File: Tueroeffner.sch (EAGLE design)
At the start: 34 parts, among them IC1 NCP1117ST33T3G, IC3 M25PE20, K1 EC2-12SNU, Q1 2N7002CK, Q3 2N7002CK

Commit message: New H-Bridge
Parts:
- removed D3, D4: PMBD914, semicon-smd-ipc:D-A1-C3
- added Q2, Q4: 2N7002CK, SparkFun-DiscreteSemi:MOSFET-NCHANNELBSS123LT1G
- added R8, R9: 100, resistor:R-EU_M2012
- R4, R5: value 47 -> 10K
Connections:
- new net N$4: R8.2, U$5.(ZEROX/IO/ADC3)P14
- new net N$5: R9.2, U$5.(TRIAC/IO/ADC2)P13
- net DC_5-12V: now also Q2.D, Q4.D; no longer D3.C, D4.C, R4.2, R5.2
- net GND: now also R4.1, R5.1
- net N$2: now also Q2.S; no longer D3.A, R4.1
- net N$3: now also Q4.S; no longer D4.A, R5.1
- net RELAY0: now also Q2.G, R4.2, R8.1; no longer U$5.(ZEROX/IO/ADC3)P14
- net RELAY1: now also Q4.G, R5.2, R9.1; no longer U$5.(TRIAC/IO/ADC2)P13
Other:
- moved on the sheet: K1, Q1, Q3, R4, R5, R6, R7

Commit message: Basic Routing
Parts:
- removed R5, R7: 10K, resistor:R-EU_M2012
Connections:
- net GND: no longer R5.1, R7.1
- net RELAY0: no longer R7.2
- net RELAY1: no longer R5.2
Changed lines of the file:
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@@
 <part name="B1" library="rectifier" deviceset="RECTIFIER-" device="S40"/>
 <part name="R6" library="resistor" deviceset="R-EU_" device="M2012" value="10K"/>
-<part name="R7" library="resistor" deviceset="R-EU_" device="M2012" value="10K"/>
 <part name="Q3" library="SparkFun-DiscreteSemi" deviceset="MOSFET-NCHANNEL" device="BSS123LT1G" value="2N7002CK"/>
 <part name="Q1" library="SparkFun-DiscreteSemi" deviceset="MOSFET-NCHANNEL" device="BSS123LT1G" value="2N7002CK"/>
@@
 <part name="JP3" library="SparkFun-Connectors" deviceset="M04" device="SCREW"/>
 <part name="R4" library="resistor" deviceset="R-EU_" device="M2012" value="10K"/>
-<part name="R5" library="resistor" deviceset="R-EU_" device="M2012" value="10K"/>
 <part name="Q2" library="SparkFun-DiscreteSemi" deviceset="MOSFET-NCHANNEL" device="BSS123LT1G" value="2N7002CK"/>
 <part name="Q4" library="SparkFun-DiscreteSemi" deviceset="MOSFET-NCHANNEL" device="BSS123LT1G" value="2N7002CK"/>
 <part name="GND8" library="supply1" deviceset="GND" device=""/>
-<part name="GND9" library="supply1" deviceset="GND" device=""/>
 <part name="GND10" library="supply1" deviceset="GND" device=""/>
 <part name="R8" library="resistor" deviceset="R-EU_" device="M2012" value="100"/>
@@
 <attribute name="VALUE" x="262.382" y="-6.35" size="1.778" layer="96" rot="R90"/>
 </instance>
-<instance part="R7" gate="G$1" x="281.94" y="-2.54" smashed="yes" rot="R90">
-<attribute name="NAME" x="280.4414" y="-6.35" size="1.778" layer="95" rot="R90"/>
-<attribute name="VALUE" x="285.242" y="-6.35" size="1.778" layer="96" rot="R90"/>
-</instance>
 <instance part="Q3" gate="G$1" x="269.24" y="5.08" smashed="yes">
 <attribute name="NAME" x="270.51" y="7.62" size="1.778" layer="95"/>
@@
 <attribute name="VALUE" x="262.382" y="24.13" size="1.778" layer="96" rot="R90"/>
 </instance>
-<instance part="R5" gate="G$1" x="281.94" y="27.94" smashed="yes" rot="R90">
-<attribute name="NAME" x="280.4414" y="24.13" size="1.778" layer="95" rot="R90"/>
-<attribute name="VALUE" x="285.242" y="24.13" size="1.778" layer="96" rot="R90"/>
-</instance>
 <instance part="Q2" gate="G$1" x="269.24" y="35.56" smashed="yes">
 <attribute name="NAME" x="270.51" y="38.1" size="1.778" layer="95"/>
@@
 <instance part="GND8" gate="1" x="259.08" y="17.78" smashed="yes">
 <attribute name="VALUE" x="256.54" y="15.24" size="1.778" layer="96"/>
-</instance>
-<instance part="GND9" gate="1" x="281.94" y="17.78" smashed="yes">
-<attribute name="VALUE" x="279.4" y="15.24" size="1.778" layer="96"/>
 </instance>
 <instance part="GND10" gate="1" x="259.08" y="-15.24" smashed="yes">
@@
 <wire x1="281.94" y1="-12.7" x2="281.94" y2="-10.16" width="0.1524" layer="91"/>
 <junction x="281.94" y="-10.16"/>
-<pinref part="R7" gate="G$1" pin="1"/>
-<wire x1="281.94" y1="-7.62" x2="281.94" y2="-10.16" width="0.1524" layer="91"/>
 <junction x="281.94" y="-10.16"/>
 <pinref part="Q3" gate="G$1" pin="S"/>
@@
 <pinref part="R4" gate="G$1" pin="1"/>
 <wire x1="259.08" y1="20.32" x2="259.08" y2="22.86" width="0.1524" layer="91"/>
-</segment>
-<segment>
-<pinref part="GND9" gate="1" pin="GND"/>
-<pinref part="R5" gate="G$1" pin="1"/>
-<wire x1="281.94" y1="20.32" x2="281.94" y2="22.86" width="0.1524" layer="91"/>
 </segment>
 <segment>
@@
 </segment>
 <segment>
-<wire x1="284.48" y1="5.08" x2="281.94" y2="5.08" width="0.1524" layer="91"/>
 <label x="279.4" y="5.08" size="0.8128" layer="95" rot="R180" xref="yes"/>
-<pinref part="R7" gate="G$1" pin="2"/>
-<wire x1="281.94" y1="5.08" x2="279.4" y2="5.08" width="0.1524" layer="91"/>
-<wire x1="281.94" y1="2.54" x2="281.94" y2="5.08" width="0.1524" layer="91"/>
-<junction x="281.94" y="5.08"/>
+<wire x1="284.48" y1="5.08" x2="279.4" y2="5.08" width="0.1524" layer="91"/>
 <pinref part="Q1" gate="G$1" pin="G"/>
 </segment>
@@
 </segment>
 <segment>
-<wire x1="284.48" y1="35.56" x2="281.94" y2="35.56" width="0.1524" layer="91"/>
 <label x="279.4" y="35.56" size="0.8128" layer="95" rot="R180" xref="yes"/>
-<pinref part="R5" gate="G$1" pin="2"/>
-<wire x1="281.94" y1="35.56" x2="279.4" y2="35.56" width="0.1524" layer="91"/>
-<wire x1="281.94" y1="33.02" x2="281.94" y2="35.56" width="0.1524" layer="91"/>
-<junction x="281.94" y="35.56"/>
+<wire x1="284.48" y1="35.56" x2="279.4" y2="35.56" width="0.1524" layer="91"/>
 <pinref part="Q4" gate="G$1" pin="G"/>
 </segment>

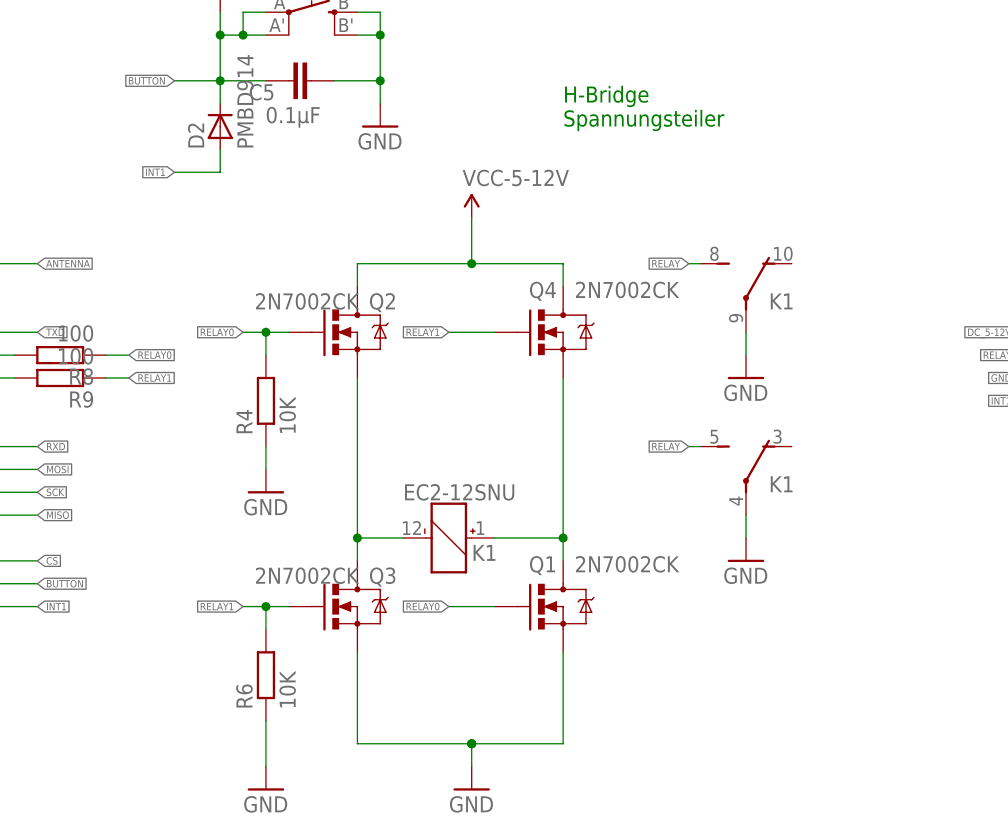
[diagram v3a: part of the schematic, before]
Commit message: New Relais designe
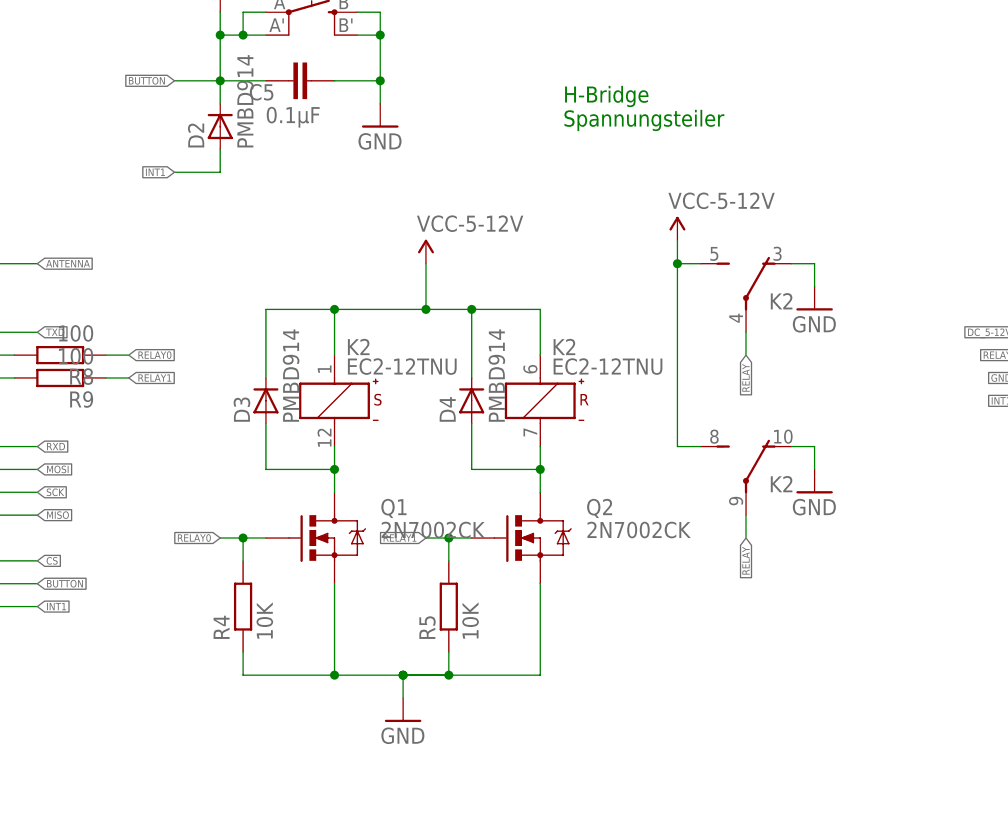
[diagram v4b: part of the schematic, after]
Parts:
- removed K1: EC2-12SNU, relay:TXD2-2M-12V
- removed Q3, Q4: 2N7002CK, SparkFun-DiscreteSemi:MOSFET-NCHANNELBSS123LT1G
- removed R6: 10K, resistor:R-EU_M2012
- added D3, D4: PMBD914, semicon-smd-ipc:D-A1-C3
- added K2: EC2-12TNU, relay:TX2-L2-12V
- added R5: 10K, resistor:R-EU_M2012
- Q1, Q2: device SparkFun-DiscreteSemi:MOSFET-NCHANNELBSS123LT1G -> SparkFun-DiscreteSemi:MOSFET-NCHANNELBSS138
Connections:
- removed net N$2: K1_.-, Q2.S, Q3.D
- removed net N$3: K1_.+, Q1.D, Q4.S
- new net N$6: D3.A, K2S.-, Q1.D
- new net N$7: D4.A, K2R.-, Q2.D
- net DC_5-12V: now also D3.C, D4.C, K21.S, K22.S, K2R.+, K2S.+; no longer Q2.D, Q4.D
- net GND: now also K21.O, K22.O, Q2.S, R5.1; no longer K1G$1.P, K1G$2.P, Q3.S, R6.1
- net RELAY: now also K21.P, K22.P; no longer K1G$1.S, K1G$2.S
- net RELAY0: no longer Q2.G
- net RELAY1: now also Q2.G, R5.2; no longer Q3.G, Q4.G, R6.2
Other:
- moved on the sheet: Q1, Q2, R4

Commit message: Semi Routed
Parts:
- C7: value 470µF 16V -> 470µF 25V
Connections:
- net AC_5-12V1: now also B1.AC1; no longer B1.AC2
- net N$1: now also B1.AC2; no longer B1.AC1
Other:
- note removed: "H-Bridge Spannungsteiler"
- moved on the sheet: JP2, R2
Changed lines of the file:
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@@
 <?xml version="1.0" encoding="utf-8"?>
 <!DOCTYPE eagle SYSTEM "eagle.dtd">
-<eagle version="7.5.0">
+<eagle version="7.4.0">
 <drawing>
 <settings>
@@
 <part name="U$1" library="adafruit" deviceset="EVQQ2" device="" value="T1"/>
 <part name="B1" library="rectifier" deviceset="RECTIFIER-" device="S40"/>
-<part name="C7" library="rcl" deviceset="CPOL-EU" device="175TMP-0810" value="470µF 16V"/>
+<part name="C7" library="rcl" deviceset="CPOL-EU" device="175TMP-0810" value="470µF 25V"/>
 <part name="JP2" library="SparkFun-Connectors" deviceset="M04" device="SCREW"/>
 <part name="JP3" library="SparkFun-Connectors" deviceset="M04" device="SCREW"/>
@@
 <sheet>
 <plain>
-<text x="292.1" y="58.42" size="1.778" layer="91">H-Bridge
-Spannungsteiler </text>
 </plain>
 <instances>
@@
 <instance part="GND2" gate="1" x="271.78" y="58.42"/>
 <instance part="P+1" gate="VCC" x="254" y="86.36"/>
-<instance part="R2" gate="G$1" x="12.7" y="22.86" rot="R180"/>
+<instance part="R2" gate="G$1" x="10.16" y="22.86" rot="R180"/>
 <instance part="D2" gate="G$1" x="254" y="58.42" rot="R90"/>
 <instance part="5-12V" gate="G$1" x="43.18" y="50.8"/>
@@
 <instance part="B1" gate="G$1" x="30.48" y="22.86"/>
 <instance part="C7" gate="G$1" x="48.26" y="25.4"/>
-<instance part="JP2" gate="G$1" x="0" y="22.86"/>
+<instance part="JP2" gate="G$1" x="-2.54" y="22.86"/>
 <instance part="JP3" gate="G$1" x="353.06" y="33.02" rot="R180"/>
 <instance part="R8" gate="G$1" x="236.22" y="33.02" smashed="yes" rot="R180">
@@
 <pinref part="IC1" gate="G$1" pin="GND"/>
 <wire x1="22.86" y1="7.62" x2="48.26" y2="7.62" width="0.1524" layer="91"/>
-<wire x1="5.08" y1="25.4" x2="22.86" y2="25.4" width="0.1524" layer="91"/>
-<label x="-5.08" y="25.4" size="0.8128" layer="95" rot="R180" xref="yes"/>
+<wire x1="2.54" y1="25.4" x2="22.86" y2="25.4" width="0.1524" layer="91"/>
+<label x="-7.62" y="25.4" size="0.8128" layer="95" rot="R180" xref="yes"/>
 <wire x1="22.86" y1="25.4" x2="22.86" y2="22.86" width="0.1524" layer="91"/>
 <pinref part="B1" gate="G$1" pin="-"/>
@@
 <wire x1="55.88" y1="27.94" x2="55.88" y2="38.1" width="0.1524" layer="91"/>
 <junction x="55.88" y="38.1"/>
-<wire x1="5.08" y1="27.94" x2="12.7" y2="27.94" width="0.1524" layer="91"/>
+<wire x1="2.54" y1="27.94" x2="12.7" y2="27.94" width="0.1524" layer="91"/>
 <wire x1="12.7" y1="27.94" x2="12.7" y2="38.1" width="0.1524" layer="91"/>
 <wire x1="12.7" y1="38.1" x2="38.1" y2="38.1" width="0.1524" layer="91"/>
-<label x="-5.08" y="27.94" size="0.8128" layer="95" rot="R180" xref="yes"/>
+<label x="-7.62" y="27.94" size="0.8128" layer="95" rot="R180" xref="yes"/>
 <wire x1="38.1" y1="38.1" x2="43.18" y2="38.1" width="0.1524" layer="91"/>
 <wire x1="43.18" y1="38.1" x2="48.26" y2="38.1" width="0.1524" layer="91"/>
@@
 <segment>
 <pinref part="R2" gate="G$1" pin="2"/>
-<wire x1="5.08" y1="22.86" x2="7.62" y2="22.86" width="0.1524" layer="91"/>
-<label x="-5.08" y="22.86" size="0.8128" layer="95" rot="R180" xref="yes"/>
+<wire x1="2.54" y1="22.86" x2="5.08" y2="22.86" width="0.1524" layer="91"/>
+<label x="-7.62" y="22.86" size="0.8128" layer="95" rot="R180" xref="yes"/>
 <pinref part="JP2" gate="G$1" pin="2"/>
 </segment>
@@
 <net name="AC_5-12V1" class="0">
 <segment>
-<wire x1="5.08" y1="20.32" x2="20.32" y2="20.32" width="0.1524" layer="91"/>
-<label x="-5.08" y="20.32" size="0.8128" layer="95" rot="R180" xref="yes"/>
-<wire x1="20.32" y1="20.32" x2="20.32" y2="15.24" width="0.1524" layer="91"/>
-<pinref part="B1" gate="G$1" pin="AC2"/>
-<wire x1="20.32" y1="15.24" x2="30.48" y2="15.24" width="0.1524" layer="91"/>
-<wire x1="30.48" y1="15.24" x2="30.48" y2="17.78" width="0.1524" layer="91"/>
+<wire x1="2.54" y1="20.32" x2="20.32" y2="20.32" width="0.1524" layer="91"/>
+<label x="-7.62" y="20.32" size="0.8128" layer="95" rot="R180" xref="yes"/>
 <pinref part="JP2" gate="G$1" pin="1"/>
-</segment>
-</net>
-<net name="N$1" class="0">
-<segment>
-<pinref part="R2" gate="G$1" pin="1"/>
-<wire x1="17.78" y1="22.86" x2="20.32" y2="22.86" width="0.1524" layer="91"/>
-<wire x1="20.32" y1="22.86" x2="20.32" y2="30.48" width="0.1524" layer="91"/>
+<wire x1="20.32" y1="20.32" x2="20.32" y2="30.48" width="0.1524" layer="91"/>
 <pinref part="B1" gate="G$1" pin="AC1"/>
 <wire x1="20.32" y1="30.48" x2="30.48" y2="30.48" width="0.1524" layer="91"/>
@@
 </segment>
 </net>
+<net name="N$1" class="0">
+<segment>
+<pinref part="R2" gate="G$1" pin="1"/>
+<wire x1="15.24" y1="22.86" x2="17.78" y2="22.86" width="0.1524" layer="91"/>
+<wire x1="17.78" y1="22.86" x2="17.78" y2="15.24" width="0.1524" layer="91"/>
+<pinref part="B1" gate="G$1" pin="AC2"/>
+<wire x1="17.78" y1="15.24" x2="30.48" y2="15.24" width="0.1524" layer="91"/>
+<wire x1="30.48" y1="15.24" x2="30.48" y2="17.78" width="0.1524" layer="91"/>
+</segment>
+</net>
 </nets>
 </sheet>
@@
 </schematic>
 </drawing>
-<compatibility>
-<note version="6.3" minversion="6.2.2" severity="warning">
-Since Version 6.2.2 text objects can contain more than one line,
-which will not be processed correctly with this version.
-</note>
-</compatibility>
 </eagle>

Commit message: RC candidate
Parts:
- removed SV3: (no value), con-lstb:MA05-2
- added TP1, TP2, TP3, TP4, TP5, TP6, TP7, TP8: TPB1,27, testpad:TPB1,27
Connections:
- net GND: now also TP4.TP; no longer SV3.7, SV3.9
- net MISO: now also TP6.TP; no longer SV3.6
- net MOSI: now also TP5.TP; no longer SV3.4
- net RESET: now also TP7.TP; no longer SV3.10
- net RXD: now also TP2.TP; no longer SV3.3
- net SCK: now also TP8.TP; no longer SV3.8
- net TXD: now also TP3.TP; no longer SV3.5
- net VCC-3.3V: now also TP1.TP; no longer SV3.1
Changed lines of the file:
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@@
 <part name="GND1" library="SparkFun-Aesthetics" deviceset="GND" device=""/>
 <part name="3.3V2" library="SparkFun-Aesthetics" deviceset="VCC" device="" value="VCC-3.3V"/>
-<part name="SV3" library="con-lstb" deviceset="MA05-2" device=""/>
 <part name="R11" library="resistor" deviceset="R-EU_" device="M2012" value="10K"/>
 <part name="3.3V8" library="SparkFun-Aesthetics" deviceset="VCC" device="" value="VCC-3.3V"/>
@@
 <part name="GND5" library="supply1" deviceset="GND" device=""/>
 <part name="5-12V2" library="SparkFun-Aesthetics" deviceset="VCC" device="" value="VCC-5-12V"/>
+<part name="TP1" library="testpad" deviceset="TP" device="B1,27"/>
+<part name="TP2" library="testpad" deviceset="TP" device="B1,27"/>
+<part name="TP3" library="testpad" deviceset="TP" device="B1,27"/>
+<part name="TP4" library="testpad" deviceset="TP" device="B1,27"/>
+<part name="TP5" library="testpad" deviceset="TP" device="B1,27"/>
+<part name="TP6" library="testpad" deviceset="TP" device="B1,27"/>
+<part name="TP7" library="testpad" deviceset="TP" device="B1,27"/>
+<part name="TP8" library="testpad" deviceset="TP" device="B1,27"/>
 </parts>
 <sheets>
@@
 <instance part="GND1" gate="1" x="177.8" y="15.24"/>
 <instance part="3.3V2" gate="G$1" x="177.8" y="35.56"/>
-<instance part="SV3" gate="G$1" x="162.56" y="76.2" rot="R180"/>
 <instance part="R11" gate="G$1" x="180.34" y="50.8" rot="R90"/>
 <instance part="3.3V8" gate="G$1" x="180.34" y="58.42"/>
@@
 <instance part="GND5" gate="1" x="320.04" y="17.78"/>
 <instance part="5-12V2" gate="G$1" x="304.8" y="45.72"/>
+<instance part="TP1" gate="G$1" x="157.48" y="81.28" rot="R270"/>
+<instance part="TP2" gate="G$1" x="157.48" y="78.74" rot="R270"/>
+<instance part="TP3" gate="G$1" x="157.48" y="76.2" rot="R270"/>
+<instance part="TP4" gate="G$1" x="157.48" y="73.66" rot="R270"/>
+<instance part="TP5" gate="G$1" x="167.64" y="78.74" rot="R90"/>
+<instance part="TP6" gate="G$1" x="167.64" y="76.2" rot="R90"/>
+<instance part="TP7" gate="G$1" x="167.64" y="71.12" rot="R90"/>
+<instance part="TP8" gate="G$1" x="167.64" y="73.66" rot="R90"/>
 </instances>
 <busses>
@@
 </segment>
 <segment>
-<pinref part="SV3" gate="G$1" pin="7"/>
+<pinref part="GND6" gate="1" pin="GND"/>
 <wire x1="154.94" y1="73.66" x2="149.86" y2="73.66" width="0.1524" layer="91"/>
-<pinref part="GND6" gate="1" pin="GND"/>
-<wire x1="149.86" y1="66.04" x2="149.86" y2="71.12" width="0.1524" layer="91"/>
-<pinref part="SV3" gate="G$1" pin="9"/>
-<wire x1="149.86" y1="71.12" x2="149.86" y2="73.66" width="0.1524" layer="91"/>
-<wire x1="154.94" y1="71.12" x2="149.86" y2="71.12" width="0.1524" layer="91"/>
-<junction x="149.86" y="71.12"/>
+<wire x1="149.86" y1="66.04" x2="149.86" y2="73.66" width="0.1524" layer="91"/>
+<pinref part="TP4" gate="G$1" pin="TP"/>
 </segment>
 <segment>
@@
 </segment>
 <segment>
-<pinref part="SV3" gate="G$1" pin="1"/>
+<pinref part="3.3V9" gate="G$1" pin="VCC"/>
 <wire x1="154.94" y1="81.28" x2="149.86" y2="81.28" width="0.1524" layer="91"/>
-<pinref part="3.3V9" gate="G$1" pin="VCC"/>
 <wire x1="149.86" y1="81.28" x2="149.86" y2="83.82" width="0.1524" layer="91"/>
+<pinref part="TP1" gate="G$1" pin="TP"/>
 </segment>
 <segment>
@@
 </segment>
 <segment>
-<pinref part="SV3" gate="G$1" pin="5"/>
+<label x="149.86" y="76.2" size="0.8128" layer="95" rot="R180" xref="yes"/>
+<pinref part="TP3" gate="G$1" pin="TP"/>
 <wire x1="154.94" y1="76.2" x2="149.86" y2="76.2" width="0.1524" layer="91"/>
-<label x="149.86" y="76.2" size="0.8128" layer="95" rot="R180" xref="yes"/>
 </segment>
 </net>
@@
 </segment>
 <segment>
-<pinref part="SV3" gate="G$1" pin="3"/>
+<label x="149.86" y="78.74" size="0.8128" layer="95" rot="R180" xref="yes"/>
+<pinref part="TP2" gate="G$1" pin="TP"/>
 <wire x1="154.94" y1="78.74" x2="149.86" y2="78.74" width="0.1524" layer="91"/>
-<label x="149.86" y="78.74" size="0.8128" layer="95" rot="R180" xref="yes"/>
 </segment>
 </net>
@@
 </segment>
 <segment>
-<pinref part="SV3" gate="G$1" pin="10"/>
+<label x="175.26" y="71.12" size="0.8128" layer="95" ratio="7" xref="yes"/>
+<pinref part="TP7" gate="G$1" pin="TP"/>
 <wire x1="170.18" y1="71.12" x2="175.26" y2="71.12" width="0.1524" layer="91"/>
-<label x="175.26" y="71.12" size="0.8128" layer="95" ratio="7" xref="yes"/>
 </segment>
 </net>
@@
 </segment>
 <segment>
-<pinref part="SV3" gate="G$1" pin="4"/>
+<label x="175.26" y="78.74" size="0.8128" layer="95" ratio="7" xref="yes"/>
+<pinref part="TP5" gate="G$1" pin="TP"/>
 <wire x1="170.18" y1="78.74" x2="175.26" y2="78.74" width="0.1524" layer="91"/>
-<label x="175.26" y="78.74" size="0.8128" layer="95" ratio="7" xref="yes"/>
 </segment>
 <segment>
@@
 </segment>
 <segment>
-<pinref part="SV3" gate="G$1" pin="8"/>
+<label x="175.26" y="73.66" size="0.8128" layer="95" ratio="7" xref="yes"/>
+<pinref part="TP8" gate="G$1" pin="TP"/>
 <wire x1="170.18" y1="73.66" x2="175.26" y2="73.66" width="0.1524" layer="91"/>
-<label x="175.26" y="73.66" size="0.8128" layer="95" ratio="7" xref="yes"/>
 </segment>
 <segment>
@@
 </segment>
 <segment>
-<pinref part="SV3" gate="G$1" pin="6"/>
+<label x="175.26" y="76.2" size="0.8128" layer="95" ratio="7" xref="yes"/>
+<pinref part="TP6" gate="G$1" pin="TP"/>
 <wire x1="170.18" y1="76.2" x2="175.26" y2="76.2" width="0.1524" layer="91"/>
-<label x="175.26" y="76.2" size="0.8128" layer="95" ratio="7" xref="yes"/>
-</segment>
-<segment>
+</segment>
+<segment>
